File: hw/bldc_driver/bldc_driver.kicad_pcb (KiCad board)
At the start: 4 copper layers, 101 x 48 mm, 159 parts, among them J1 430450412, J2 B6B-EH-A(LF)(SN), J3 B4B-EH-A(LF)(SN), J4 1733583, Q2 IRF540N, Q3 IRF540N, Q4 IRF540N, Q5 IRF540N, Q6 IRF540N, Q7 IRF540N, SW1 BTSA-N-P-1, U10 TPS54202DDC, U11 AMC1200BDWV, U12 AMC1200BDWV, U13 AMC1200BDWV, U14 SN65HVD230, U15 STM32L431CCTx, U16 SN74LVC1G125DBV, U17 SN74LVC1G125DBV, U2 STGAP2SCM, U3 STGAP2SCM, U4 STGAP2SCM, U5 STGAP2SCM, U6 STGAP2SCM, U7 STGAP2SCM, U8 TPS54202DDC, U9 AMC1200BDWV, Y1 Crystal_GND24

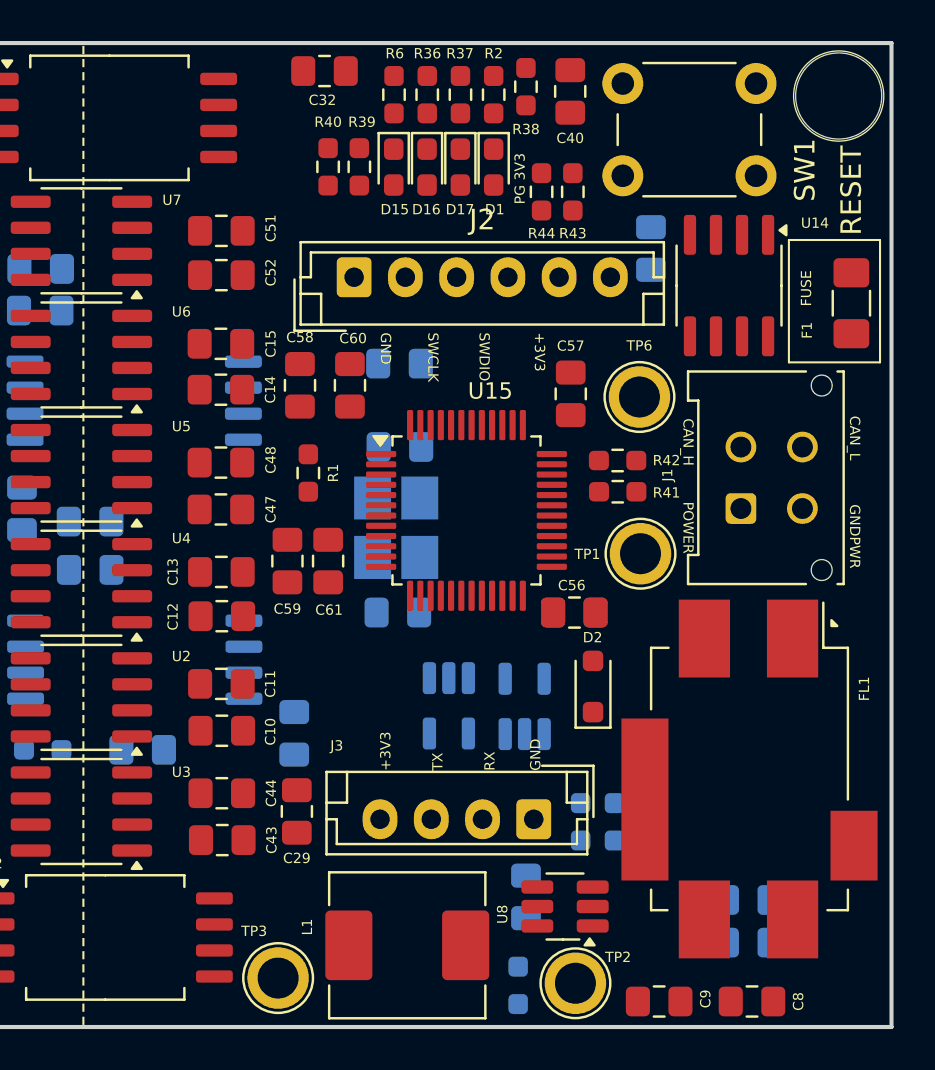
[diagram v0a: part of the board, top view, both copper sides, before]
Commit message: half routed
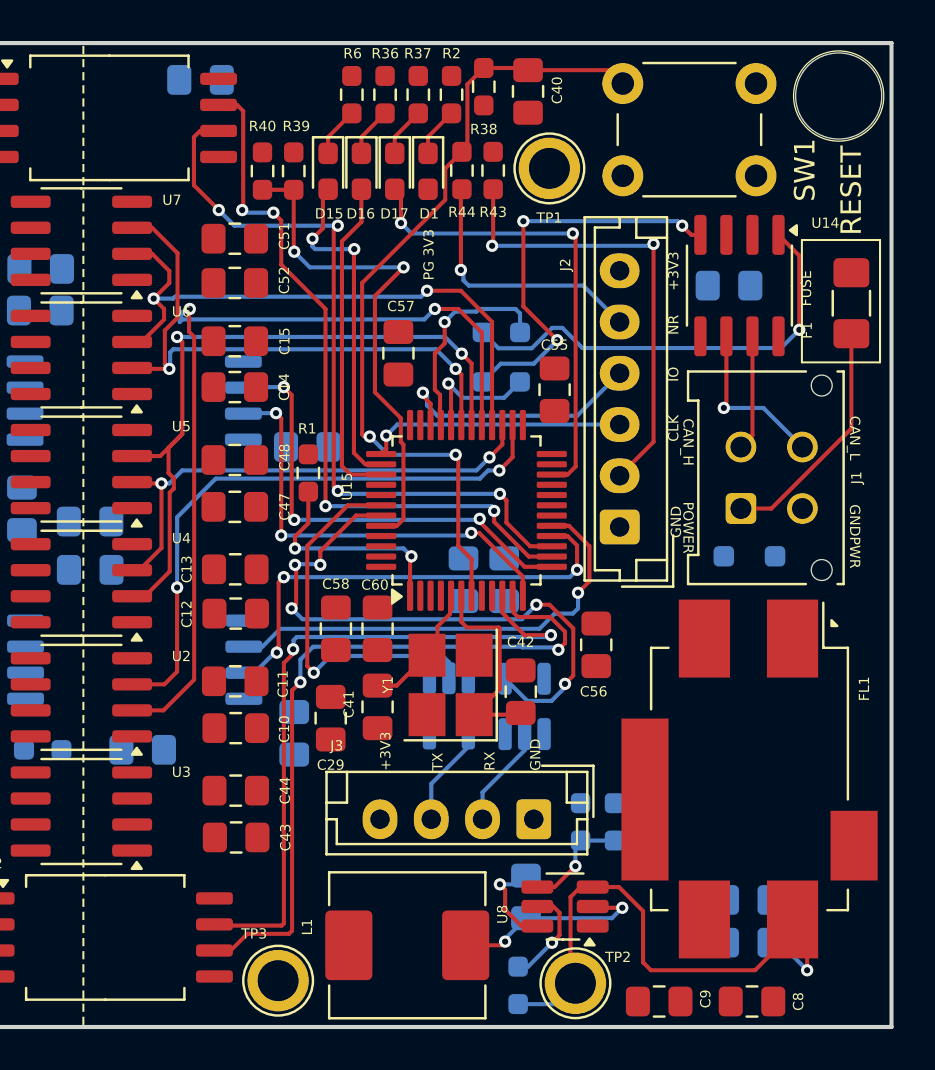
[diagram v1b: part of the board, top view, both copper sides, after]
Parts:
- removed TP6: TestPoint_Flag, TestPoint:TestPoint_Plated_Hole_D2.0mm
- C32, C59, C61, D2, R41, R42: moved to B.Cu
- C41, C42, C55, Y1: moved to F.Cu
- moved TP1 19.3 mm to (155.8, 73.5)
- moved J2 17.8 mm to (159.3, 91.0), turned to 90 degrees
- moved C41 12.7 mm to (147.4, 99.8), turned to 90 degrees
- moved C58 12.0 mm to (145.4, 96.0), turned to 90 degrees
- moved C60 12.0 mm to (147.4, 96.0), turned to 90 degrees
- moved C55 10.9 mm to (156.1, 84.3), turned to 90 degrees
- moved D2 9.93 mm to (165.6, 92.5), turned to 180 degrees
- moved C57 8.64 mm to (148.5, 82.5)
- moved C59 8.64 mm to (151.6, 93.6), turned to -90 degrees
- moved C61 8.64 mm to (153.6, 93.6), turned to -90 degrees
- moved R42 8.44 mm to (153.5, 81.5), turned to 0 degrees
- moved Y1 8.12 mm to (151.0, 98.7)
- moved R41 7.81 mm to (153.5, 83.9), turned to 180 degrees
- moved C42 7.13 mm to (154.4, 99.1), turned to -90 degrees
- moved C32 6.06 mm to (138.8, 69.2), turned to 0 degrees
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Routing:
- net /PH_U_HI: track 0.00 -> 42.4 mm, vias 0 -> 2
- net /NRESET: track 0.00 -> 39.6 mm, vias 0 -> 2
- net /W_ADC_N: track 0.00 -> 36.8 mm, vias 0 -> 4
- net /W_ADC_P: track 0.00 -> 35.6 mm, vias 0 -> 4
- net /U_ADC_N: track 0.00 -> 35.2 mm, vias 0 -> 2
- net /PH_V_HI: track 0.00 -> 35.1 mm, vias 0 -> 2
- net /U_ADC_P: track 0.00 -> 33.8 mm, vias 0 -> 2
- net Net-(FL1-CB): track 0.00 -> 30.4 mm, vias 0 -> 1
- net /PH_W_LO: track 0.00 -> 29.4 mm, vias 0 -> 2
- net Net-(U15-PB7): track 0.00 -> 29.3 mm, vias 0 -> 5
- net /PH_U_LO: track 0.00 -> 29.1 mm, vias 0 -> 2
- net /PH_W_HI: track 0.00 -> 29.0 mm, vias 0 -> 2
- net Net-(U15-PH3): track 0.00 -> 24.9 mm, vias 0 -> 2
- net /PH_V_LO: track 0.00 -> 24.8 mm, vias 0 -> 2
- net Net-(D17-A): track 0.00 -> 23.1 mm, vias 0 -> 2
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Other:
- board text added: "CLK"
- board text added: "IO"
- board text added: "NR"
- board text removed: "SWCLK"
- board text removed: "SWDIO"

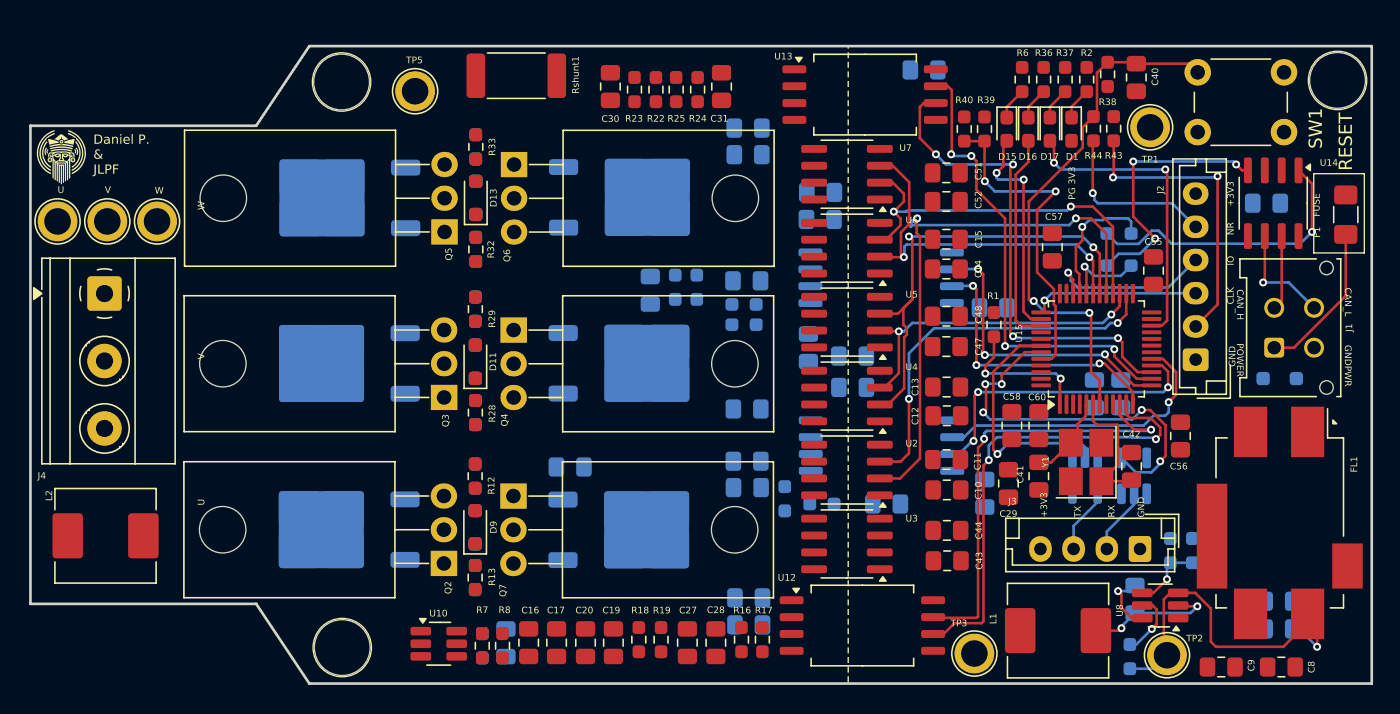
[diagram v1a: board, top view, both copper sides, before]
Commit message: half routed
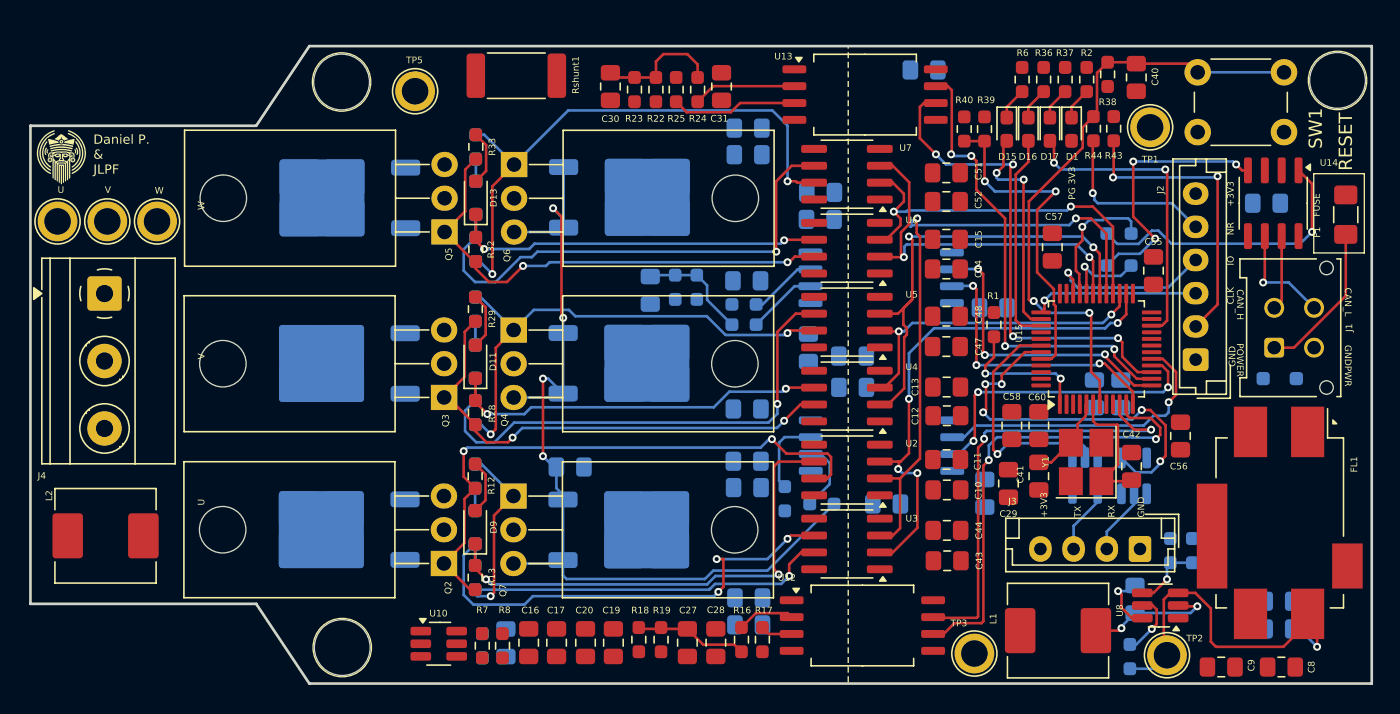
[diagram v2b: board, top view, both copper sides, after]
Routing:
- net Net-(Q4-S): track 0.00 -> 72.6 mm, vias 0 -> 4
- net Net-(Q2-G): track 0.00 -> 44.3 mm, vias 0 -> 2
- net Net-(Q6-G): track 0.00 -> 43.4 mm, vias 0 -> 2
- net Net-(Q7-G): track 0.00 -> 40.9 mm, vias 0 -> 2
- net Net-(D12-K): track 0.00 -> 38.5 mm, vias 0 -> 1
- net Net-(Q4-G): track 0.00 -> 38.1 mm, vias 0 -> 2
- net Net-(D14-K): track 0.00 -> 38.1 mm, vias 0 -> 1
- net Net-(Q3-G): track 0.00 -> 37.4 mm, vias 0 -> 2
- net Net-(Q5-G): track 0.00 -> 37.0 mm, vias 0 -> 2
- net Net-(D9-K): track 0.00 -> 37.0 mm, vias 0 -> 2
- net Net-(D10-K): track 0.00 -> 36.9 mm, vias 0 -> 3
- net Net-(D11-K): track 0.00 -> 28.5 mm, vias 0 -> 2
- net Net-(D13-K): track 0.00 -> 28.0 mm, vias 0 -> 2
- net /PH_U_LO: track 29.1 -> 39.0 mm, vias 2 -> 4
- net Net-(R25-Pad2): track 0.00 -> 9.51 mm
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
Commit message: full route
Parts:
- removed R1: 0 ohm, Resistor_SMD:R_0603_1608Metric_Pad0.98x0.95mm_HandSolder
- added C62: 0.1 µF, Capacitor_SMD:C_0805_2012Metric_Pad1.18x1.45mm_HandSolder, B.Cu at (147.4, 99.8)
- added C63: 0.1 µF, Capacitor_SMD:C_0805_2012Metric_Pad1.18x1.45mm_HandSolder, B.Cu at (158.0, 100.3)
- C29, C56, C8: moved to B.Cu
- C32: moved to F.Cu
- moved C54 35.9 mm to (130.7, 75.4), turned to 0 degrees
- moved C45 35.7 mm to (129.8, 111.0)
- moved C46 35.7 mm to (129.8, 109.0)
- moved C53 31.9 mm to (130.7, 77.5), turned to 0 degrees
- moved C35 19.3 mm to (125.5, 108.3), turned to 180 degrees
- moved C33 14.7 mm to (130.6, 93.1)
- moved C8 11.2 mm to (154.6, 113.0), turned to -90 degrees
- moved C29 9.10 mm to (142.6, 109.1), turned to 180 degrees
- moved C56 8.15 mm to (156.5, 88.8)
- moved R3 7.40 mm to (161.7, 113.8), turned to 180 degrees
- moved C9 6.98 mm to (154.3, 113.0), turned to -90 degrees
- moved C36 6.20 mm to (127.5, 91.3), turned to 90 degrees
- moved C25 5.70 mm to (125.5, 81.9), turned to 0 degrees
- moved C21 5.69 mm to (130.3, 101.7)
- moved C32 4.54 mm to (143.0, 71.0), turned to 180 degrees
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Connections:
- C33 pad 2: GND -> GNDPWR
- C34 pad 2: GND -> GNDPWR
- C35 pad 2: GND -> GNDPWR
- C36 pad 2: GND -> GNDPWR
- C37 pad 2: GND -> GNDPWR
- C38 pad 2: GND -> GNDPWR
- C45 pad 2: GND -> GNDPWR
- C46 pad 2: GND -> GNDPWR
- C49 pad 2: GND -> GNDPWR
- C50 pad 2: GND -> GNDPWR
- C53 pad 2: GND -> GNDPWR
- C54 pad 2: GND -> GNDPWR
- D2 pad 2: +VDC -> Net-(D2-A2)
- F1 pad 2: Net-(J1-Pin_1) -> Net-(D2-A2)
- J1 pad 1: Net-(J1-Pin_1) -> Net-(D2-A2)
- U15 pad 1: Net-(U15-VBAT) -> +3V3
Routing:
- net +VDC: track 0.00 -> 174.0 mm, vias 0 -> 32
- net +5V: track 0.00 -> 156.4 mm, vias 0 -> 9
- net GND: track 0.00 -> 138.6 mm, vias 0 -> 49
- net +3V3: track 0.00 -> 134.6 mm, vias 0 -> 26
- net GNDPWR: track 0.00 -> 102.8 mm, vias 0 -> 31
- net /Motor/MOTOR_U: track 0.39 -> 77.2 mm, vias 0 -> 11
- net /Motor/MOTOR_V: track 0.78 -> 47.5 mm, vias 0 -> 5
- net Net-(U10-SW): track 0.00 -> 37.4 mm, vias 0 -> 1
- net /Motor/MOTOR_W: track 2.63 -> 38.1 mm, vias 0 -> 7
- net Net-(U8-SW): track 9.94 -> 28.1 mm
- net Net-(D2-A2): track 0.00 -> 14.2 mm
- net Net-(J1-Pin_1): track 11.6 -> 0.00 mm
- net Net-(U15-VBAT): track 10.8 -> 0.00 mm, vias 2 -> 0
- net Net-(U10-BOOT): track 0.00 -> 9.78 mm, vias 0 -> 1
- net Net-(U10-FB): track 0.00 -> 7.22 mm, vias 0 -> 1
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- added copper zone on In1.Cu, net +3V3
- added copper zone on In1.Cu, net +VDC
- added copper zone on In1.Cu, net /Motor/MOTOR_U
- added copper zone on In1.Cu, net /Motor/MOTOR_V
- added copper zone on In1.Cu, net /Motor/MOTOR_W
- added copper zone on In2.Cu, net GND
- added copper zone on In2.Cu, net GNDPWR
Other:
- outline, holes or cut-outs redrawn

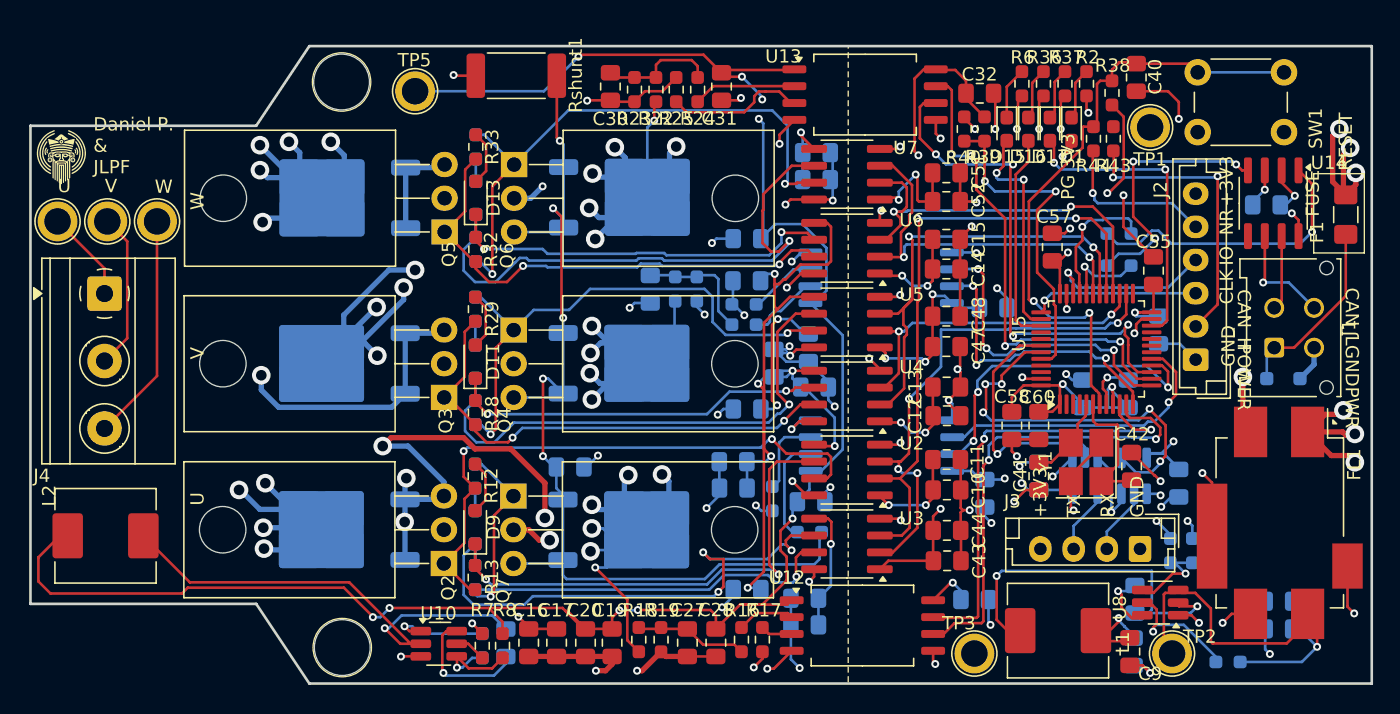
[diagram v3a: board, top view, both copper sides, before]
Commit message: fmu: update power supply and other connections
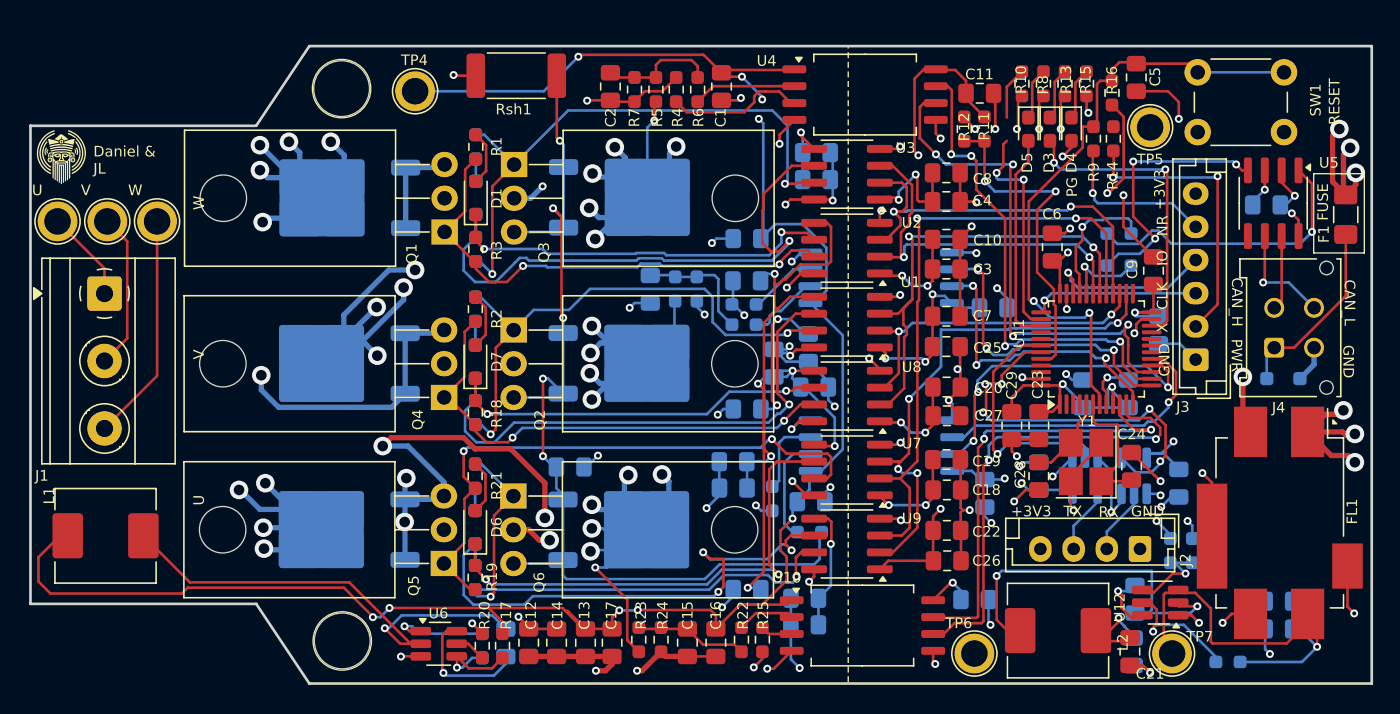
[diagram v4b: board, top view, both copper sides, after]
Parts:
- removed the D15 at (145.0, 73.7)
- renumbered C31 to C1, C15 to C10, C32 to C11, C16 to C12, C20 to C13, C17 to C14, C27 to C15, C28 to C16, C19 to C17, C10 to C18, C11 to C19, C30 to C2, C13 to C20, C9 to C21, C44 to C22, C60 to C23, C42 to C24, C47 to C25, C43 to C26, C12 to C27, C41 to C28, C58 to C29, C14 to C3, C39 to C30, C26 to C31, C56 to C32, C24 to C33, C53 to C34, C25 to C35, C54 to C36, C34 to C37, C6 to C38, C5 to C39, C52 to C4, C62 to C40, C29 to C41, C22 to C42, C8 to C43, C7 to C44, C61 to C45, C63 to C46, C59 to C47, C21 to C48, C50 to C49, C40 to C5, C33 to C50, C46 to C51, C38 to C52, C36 to C53, C49 to C54, C45 to C55, C35 to C56, C37 to C57, C23 to C58, C18 to C59, C57 to C6, C48 to C7, C51 to C8, C55 to C9, D13 to D1, D14 to D10, D2 to D11, D6 to D12, D4 to D13, D5 to D14, D3 to D15, D10 to D16, D12 to D17, D17 to D3, D1 to D4, D16 to D5, D9 to D6, D11 to D7, D7 to D9, J4 to J1, J3 to J2, J2 to J3, J1 to J4, L2 to L1, L1 to L2, Q5 to Q1, Q4 to Q2, Q6 to Q3, Q3 to Q4, Q2 to Q5, Q7 to Q6, R33 to R1, R6 to R10, R39 to R11, R40 to R12, R37 to R13, R43 to R14, R2 to R15, R38 to R16, R8 to R17, R28 to R18, R13 to R19, R29 to R2, R7 to R20, R12 to R21, R16 to R22, R18 to R23, R19 to R24, R17 to R25, R41 to R26, R42 to R27, R21 to R28, R20 to R29, R32 to R3, R15 to R30, R14 to R31, R35 to R32, R34 to R33, R31 to R34, R5 to R35, R4 to R36, R3 to R37, R10 to R38, R11 to R39, R25 to R4, R26 to R40, R30 to R41, R27 to R42, R9 to R43, R22 to R5, R24 to R6, R23 to R7, R36 to R8, R44 to R9, Rshunt1 to Rsh1, TP8 to TP1, TP9 to TP2, TP7 to TP3, TP5 to TP4, TP1 to TP5, TP3 to TP6, TP2 to TP7, U5 to U1, U12 to U10, U15 to U11, U8 to U12, U11 to U13, U16 to U14, U17 to U15, U9 to U16, U6 to U2, U7 to U3, U13 to U4, U14 to U5, U10 to U6, U2 to U7, U4 to U8, U3 to U9
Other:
- outline, holes or cut-outs redrawn
- board text added: "Daniel & JL"
- board text added: "PG"
- board text added: "PWR"
- board text added: "X"
- board text removed: "Daniel P. & JLPF"
- board text removed: "GNDPWR"
- board text removed: "PG 3V3"
- board text removed: "POWER"
